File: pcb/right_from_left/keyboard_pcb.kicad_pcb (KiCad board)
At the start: 2 copper layers, 138.8 x 89.9 mm, 47 parts, among them J1 TRRS, J2 Conn_01x04_Male, K0 KEYSW, K1 KEYSW, K10 KEYSW, K11 KEYSW, K12 KEYSW, K13 KEYSW, K14 KEYSW, K15 KEYSW, K2 KEYSW, K20 KEYSW, K21 KEYSW, K22 KEYSW, K23 KEYSW, K24 KEYSW, K25 KEYSW, K3 KEYSW, K30 KEYSW, K31 KEYSW, K32 KEYSW, K4 KEYSW, K5 KEYSW, U1 PCF8574, U2 Pico

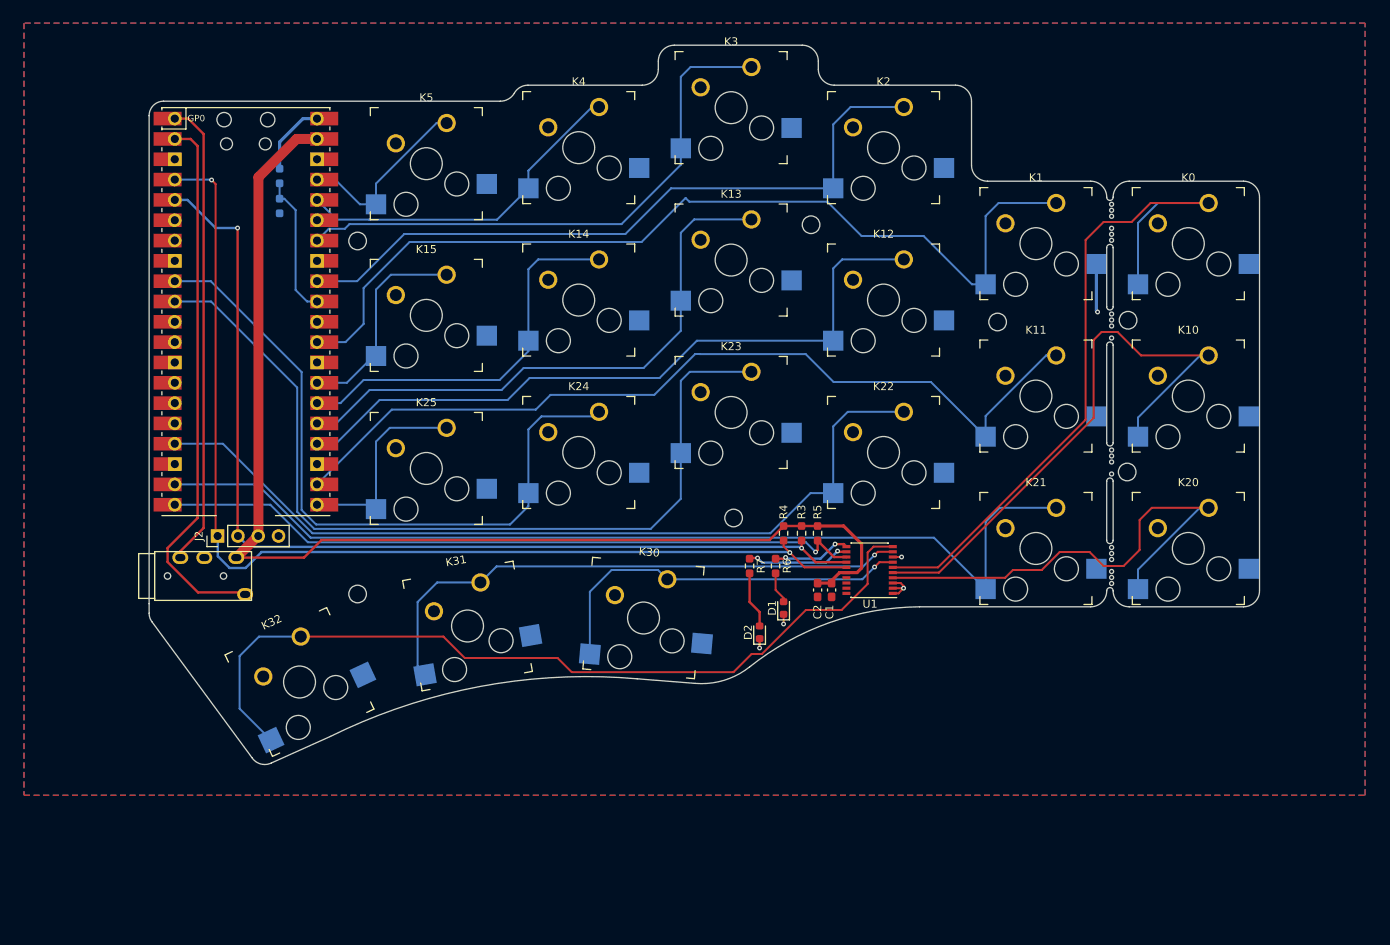
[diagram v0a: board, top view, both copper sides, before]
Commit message: right_from_left is ready for review
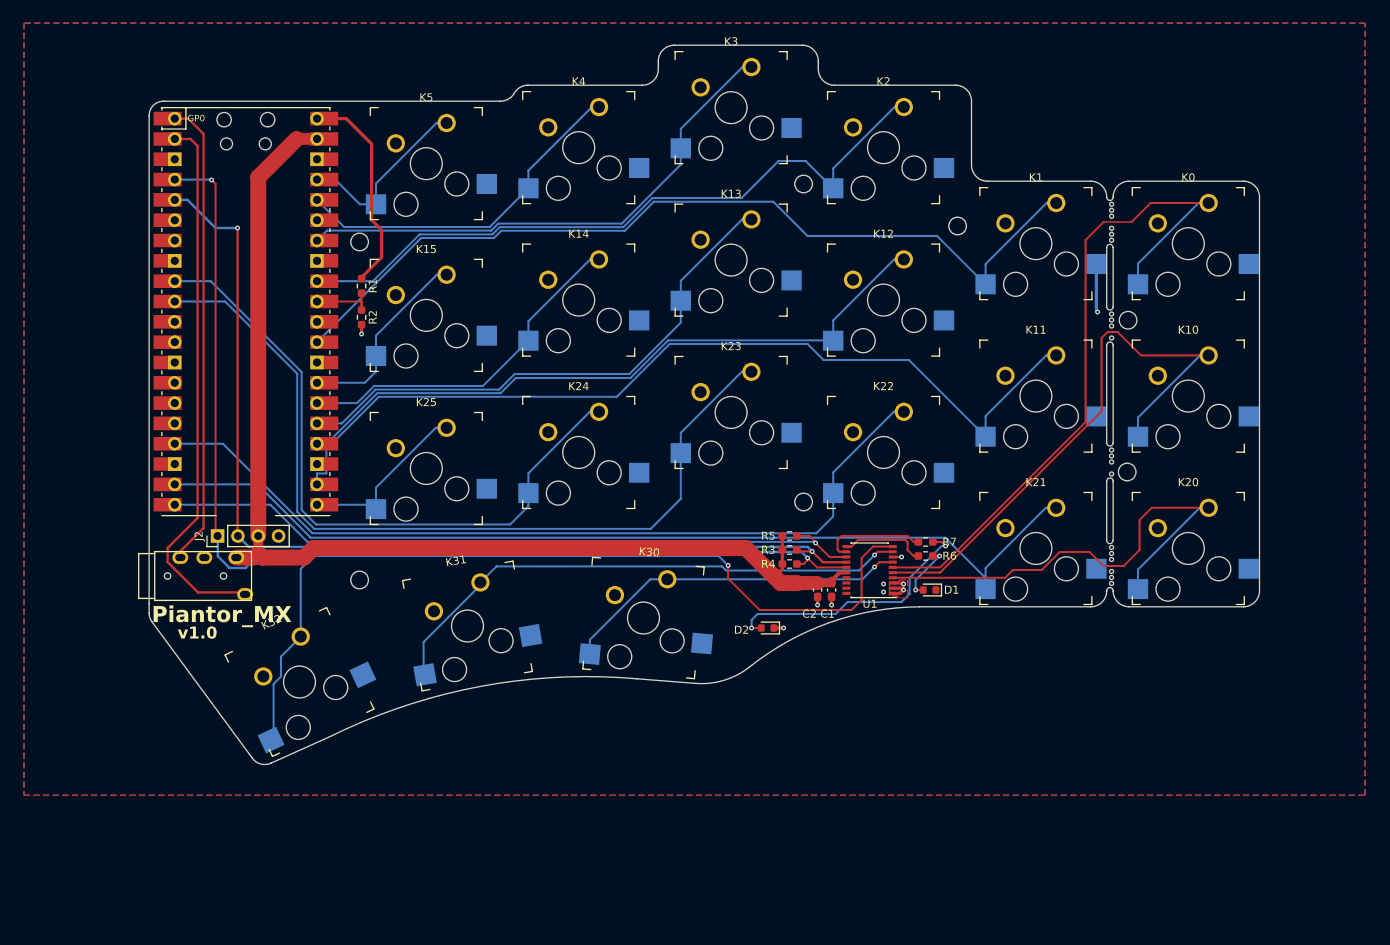
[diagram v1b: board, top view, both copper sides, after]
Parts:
- R1, R2: moved to F.Cu
- R3, R4: value R -> 4k7
- moved H1 29.8 mm to (148.2, 60.8)
- moved R7 22.2 mm to (163.5, 105.5), turned to 0 degrees
- moved R6 18.8 mm to (163.5, 107.2), turned to 0 degrees
- moved D1 18.4 mm to (164.0, 111.5), turned to 180 degrees
- moved H1 18.3 mm to (167.5, 66.0)
- moved R2 17.3 mm to (93.0, 77.4)
- moved R1 17.2 mm to (93.0, 73.5)
- moved H4 8.98 mm to (148.2, 100.5)
- moved R4 3.91 mm to (146.5, 108.2), turned to 0 degrees
- moved R5 3.52 mm to (146.5, 104.8), turned to 0 degrees
- moved R3 2.57 mm to (146.5, 106.5), turned to 0 degrees
- moved H3 1.77 mm to (92.8, 110.2)
- moved D2 1.14 mm to (143.8, 116.2), turned to 180 degrees
- moved H2 0.28 mm to (92.8, 68.0)
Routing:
- net Net-(D2-A): track 7.11 -> 33.3 mm, vias 0 -> 2
- net VBUS: track 9.22 -> 26.8 mm
- net vbus_sense: track 17.8 -> 8.69 mm
- net VCC: track 148.2 -> 141.6 mm
- net /k01: track 116.2 -> 109.6 mm
- net /k14: track 48.7 -> 44.1 mm
- net /k30: track 47.7 -> 43.2 mm
- net /k13: track 72.0 -> 67.9 mm
- net /k03: track 69.7 -> 65.9 mm
- net /k12: track 88.2 -> 84.4 mm
- net /k11: track 109.2 -> 112.8 mm
- net /k31: track 71.5 -> 68.1 mm
- net /k25: track 25.6 -> 22.2 mm
- net Net-(D1-A): track 3.96 -> 7.29 mm, vias 0 -> 2
- net /k24: track 87.2 -> 84.0 mm
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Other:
- board text added: "Piantor_MX"
- board text added: "v1.0"

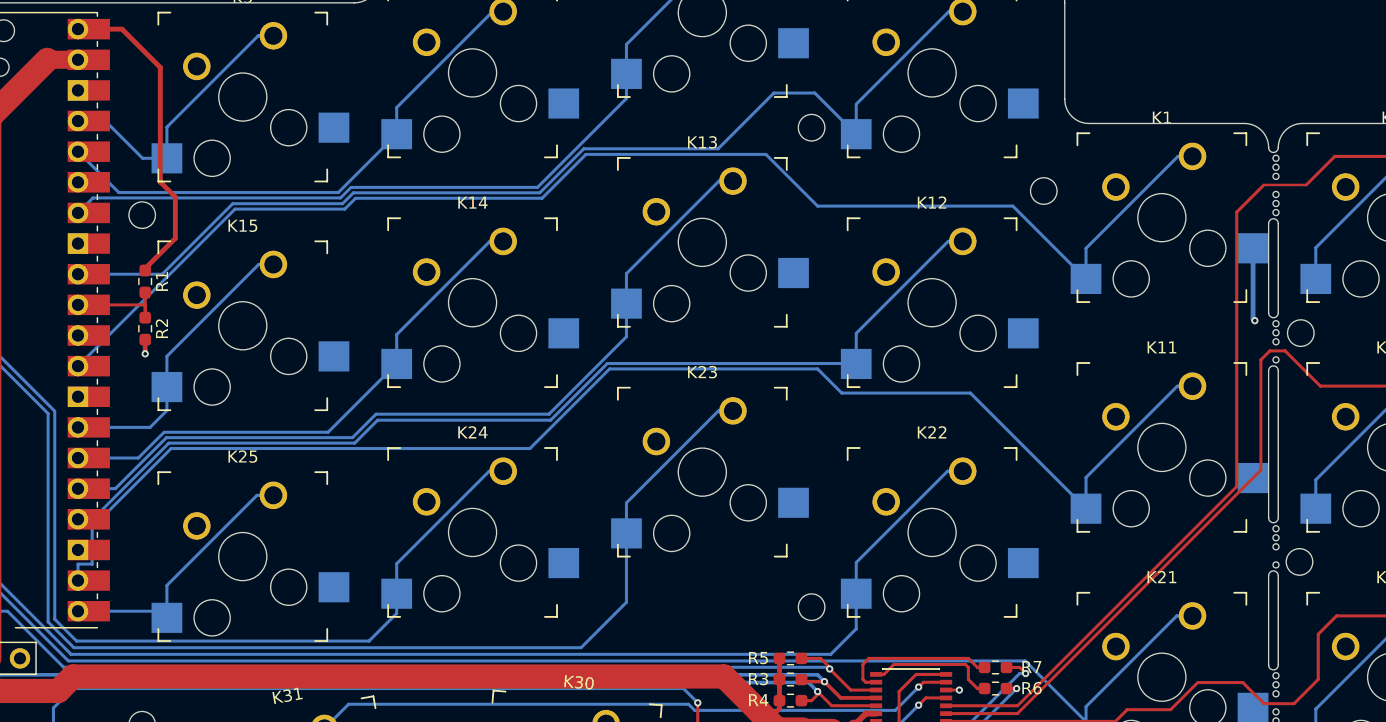
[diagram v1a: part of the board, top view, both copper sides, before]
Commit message: Mechanical parts are "mirrored", ToDo: Pin header LCD i2c pinheader needs alignment
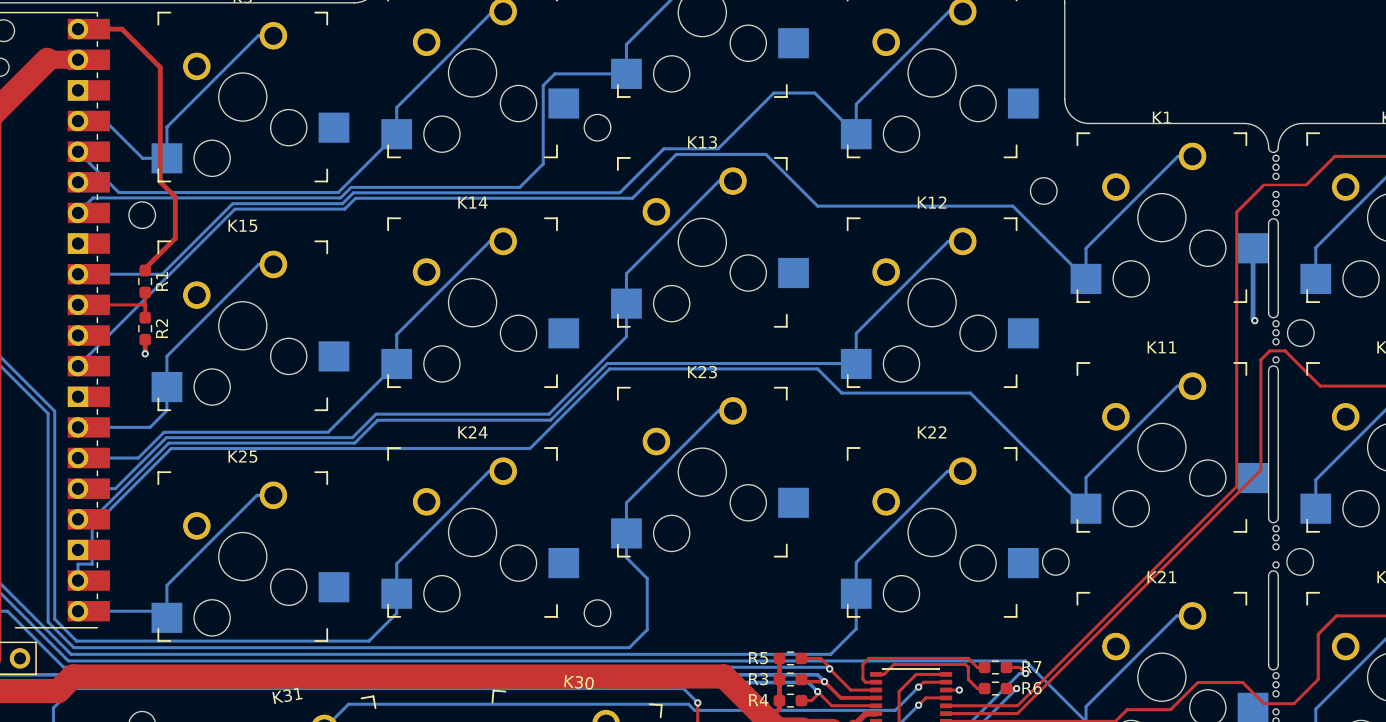
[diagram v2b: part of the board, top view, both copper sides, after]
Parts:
- added H4: MountingHole, beekeeb_lib:MountingHole_2.2mm_M2-8mm, B.Cu at (130.5, 101.0)
- moved H4 20.6 mm to (168.5, 96.8)
- moved H1 17.8 mm to (130.5, 60.8)
- moved H4 0.06 mm to (188.8, 96.8)
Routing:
- net /k23: track 106.9 -> 110.7 mm
- net /k03: track 65.9 -> 68.5 mm
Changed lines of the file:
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@@
   )
   (footprint "beekeeb_lib:MountingHole_2.2mm_M2-8mm" (layer "B.Cu")
-    (at 148.25 100.5 180)
+    (at 168.5 96.75 180)
     (descr "Mounting Hole 2.2mm, no annular, M2")
     (tags "mounting hole 2.2mm no annular m2")
@@
   )
   (footprint "beekeeb_lib:MountingHole_2.2mm_M2-8mm" (layer "B.Cu")
-    (at 188.75 96.75 180)
+    (at 188.808 96.75 180)
     (descr "Mounting Hole 2.2mm, no annular, M2")
     (tags "mounting hole 2.2mm no annular m2")
@@
   )
   (footprint "beekeeb_lib:MountingHole_2.2mm_M2-8mm" (layer "B.Cu")
-    (at 148.25 60.75 180)
+    (at 130.5 101 180)
+    (descr "Mounting Hole 2.2mm, no annular, M2")
+    (tags "mounting hole 2.2mm no annular m2")
+    (property "Sheetfile" "keyboard_pcb.kicad_sch")
+    (property "Sheetname" "")
+    (property "ki_description" "Mounting Hole without connection")
+    (property "ki_keywords" "mounting hole")
+    (attr exclude_from_pos_files)
+    (fp_text reference "H4" (at 0 3.2) (layer "B.SilkS") hide
+        (effects (font (size 1 1) (thickness 0.15)) (justify mirror))
+    )
+    (fp_text value "MountingHole" (at 2.335 -4.852) (layer "B.Fab")
+        (effects (font (size 1 1) (thickness 0.15)) (justify mirror))
+    )
+    (fp_text user "${REFERENCE}" (at 0 0) (layer "B.Fab")
+        (effects (font (size 1 1) (thickness 0.15)) (justify mirror))
+    )
+    (fp_circle (center 0 0) (end 2.2 0)
+      (stroke (width 0.15) (type solid)) (fill none) (layer "Cmts.User"))
+    (fp_circle (center 0 0) (end 4 0)
+      (stroke (width 0.05) (type solid)) (fill none) (layer "B.CrtYd"))
+    (pad "" np_thru_hole circle (at 0 0 180) (size 2.2 2.2) (drill 2.2) (layers "*.Cu" "*.Mask"))
+  )
+  (footprint "beekeeb_lib:MountingHole_2.2mm_M2-8mm" (layer "B.Cu")
+    (at 130.5 60.75 180)
     (descr "Mounting Hole 2.2mm, no annular, M2")
     (tags "mounting hole 2.2mm no annular m2")
@@
   (segment (start 197.622 63.128) (end 198.88 63.128) (width 0.25) (layer "B.Cu") (net 2))
   (segment (start 190.05 70.7) (end 197.622 63.128) (width 0.25) (layer "B.Cu") (net 2))
-  (segment (start 100.4448 67.5) (end 109.54507 67.5) (width 0.25) (layer "B.Cu") (net 3))
-  (segment (start 110.446567 66.598503) (end 125.901497 66.598503) (width 0.25) (layer "B.Cu") (net 3))
-  (segment (start 170.975 73.288) (end 171 73.288) (width 0.25) (layer "B.Cu") (net 3))
+  (segment (start 137.037 62.963) (end 144.463 62.963) (width 0.25) (layer "B.Cu") (net 3))
+  (segment (start 110.446567 66.598503) (end 133.401497 66.598503) (width 0.25) (layer "B.Cu") (net 3))
   (segment (start 109.54507 67.5) (end 110.446567 66.598503) (width 0.25) (layer "B.Cu") (net 3))
   (segment (start 148.75 67.25) (end 164.937 67.25) (width 0.25) (layer "B.Cu") (net 3))
-  (segment (start 125.901497 66.598503) (end 129.537 62.963) (width 0.25) (layer "B.Cu") (net 3))
+  (segment (start 170.975 73.288) (end 171 73.288) (width 0.25) (layer "B.Cu") (net 3))
+  (segment (start 100.4448 67.5) (end 109.54507 67.5) (width 0.25) (layer "B.Cu") (net 3))
+  (segment (start 87.4268 80.518) (end 100.4448 67.5) (width 0.25) (layer "B.Cu") (net 3))
+  (segment (start 144.463 62.963) (end 148.75 67.25) (width 0.25) (layer "B.Cu") (net 3))
+  (segment (start 133.401497 66.598503) (end 137.037 62.963) (width 0.25) (layer "B.Cu") (net 3))
   (segment (start 164.937 67.25) (end 170.975 73.288) (width 0.25) (layer "B.Cu") (net 3))
-  (segment (start 144.463 62.963) (end 148.75 67.25) (width 0.25) (layer "B.Cu") (net 3))
-  (segment (start 87.4268 80.518) (end 100.4448 67.5) (width 0.25) (layer "B.Cu") (net 3))
-  (segment (start 129.537 62.963) (end 144.463 62.963) (width 0.25) (layer "B.Cu") (net 3))
   (segment (start 171 70.75) (end 178.622 63.128) (width 0.25) (layer "B.Cu") (net 3))
   (segment (start 178.622 63.128) (end 179.83 63.128) (width 0.25) (layer "B.Cu") (net 3))
   (segment (start 171 73.288) (end 171 70.75) (width 0.25) (layer "B.Cu") (net 3))
+  (segment (start 140.5 62.5) (end 145.125 57.875) (width 0.25) (layer "B.Cu") (net 4))
   (segment (start 151.95 61.288) (end 151.95 58.8) (width 0.25) (layer "B.Cu") (net 4))
-  (segment (start 140.5 62.5) (end 145.125 57.875) (width 0.25) (layer "B.Cu") (net 4))
+  (segment (start 148.512 57.875) (end 151.925 61.288) (width 0.25) (layer "B.Cu") (net 4))
+  (segment (start 109.358881 67.050499) (end 110.260378 66.149002) (width 0.25) (layer "B.Cu") (net 4))
   (segment (start 145.125 57.875) (end 148.512 57.875) (width 0.25) (layer "B.Cu") (net 4))
+  (segment (start 132.350998 66.149002) (end 136 62.5) (width 0.25) (layer "B.Cu") (net 4))
   (segment (start 94.41111 72.898) (end 100.258611 67.050499) (width 0.25) (layer "B.Cu") (net 4))
-  (segment (start 148.512 57.875) (end 151.925 61.288) (width 0.25) (layer "B.Cu") (net 4))
   (segment (start 151.925 61.288) (end 151.95 61.288) (width 0.25) (layer "B.Cu") (net 4))
-  (segment (start 109.358881 67.050499) (end 110.260378 66.149002) (width 0.25) (layer "B.Cu") (net 4))
-  (segment (start 110.260378 66.149002) (end 125.715308 66.149002) (width 0.25) (layer "B.Cu") (net 4))
+  (segment (start 136 62.5) (end 140.5 62.5) (width 0.25) (layer "B.Cu") (net 4))
+  (segment (start 159.622 51.128) (end 160.78 51.128) (width 0.25) (layer "B.Cu") (net 4))
+  (segment (start 100.258611 67.050499) (end 109.358881 67.050499) (width 0.25) (layer "B.Cu") (net 4))
+  (segment (start 151.95 58.8) (end 159.622 51.128) (width 0.25) (layer "B.Cu") (net 4))
   (segment (start 87.4268 72.898) (end 94.41111 72.898) (width 0.25) (layer "B.Cu") (net 4))
-  (segment (start 159.622 51.128) (end 160.78 51.128) (width 0.25) (layer "B.Cu") (net 4))
-  (segment (start 151.95 58.8) (end 159.622 51.128) (width 0.25) (layer "B.Cu") (net 4))
-  (segment (start 125.715308 66.149002) (end 129.36431 62.5) (width 0.25) (layer "B.Cu") (net 4))
-  (segment (start 100.258611 67.050499) (end 109.358881 67.050499) (width 0.25) (layer "B.Cu") (net 4))
-  (segment (start 129.36431 62.5) (end 140.5 62.5) (width 0.25) (layer "B.Cu") (net 4))
+  (segment (start 110.260378 66.149002) (end 132.350998 66.149002) (width 0.25) (layer "B.Cu") (net 4))
+  (segment (start 124.050499 65.699501) (end 126 63.75) (width 0.25) (layer "B.Cu") (net 5))
+  (segment (start 109.19869 66.575) (end 110.074189 65.699501) (width 0.25) (layer "B.Cu") (net 5))
+  (segment (start 132.9 53.85) (end 140.622 46.128) (width 0.25) (layer "B.Cu") (net 5))
   (segment (start 88.6698 66.575) (end 109.19869 66.575) (width 0.25) (layer "B.Cu") (net 5))
-  (segment (start 132.9 53.85) (end 140.622 46.128) (width 0.25) (layer "B.Cu") (net 5))
+  (segment (start 126 57.25) (end 126.962 56.288) (width 0.25) (layer "B.Cu") (net 5))
+  (segment (start 126.962 56.288) (end 132.9 56.288) (width 0.25) (layer "B.Cu") (net 5))
+  (segment (start 126 63.75) (end 126 57.25) (width 0.25) (layer "B.Cu") (net 5))
+  (segment (start 132.9 56.288) (end 132.9 53.85) (width 0.25) (layer "B.Cu") (net 5))
+  (segment (start 110.074189 65.699501) (end 124.050499 65.699501) (width 0.25) (layer "B.Cu") (net 5))
   (segment (start 87.4268 67.818) (end 88.6698 66.575) (width 0.25) (layer "B.Cu") (net 5))
-  (segment (start 132.9 56.288) (end 132.9 53.85) (width 0.25) (layer "B.Cu") (net 5))
-  (segment (start 110.074189 65.699501) (end 125.529119 65.699501) (width 0.25) (layer "B.Cu") (net 5))
-  (segment (start 109.19869 66.575) (end 110.074189 65.699501) (width 0.25) (layer "B.Cu") (net 5))
-  (segment (start 125.529119 65.699501) (end 132.9 58.32862) (width 0.25) (layer "B.Cu") (net 5))
-  (segment (start 132.9 58.32862) (end 132.9 56.288) (width 0.25) (layer "B.Cu") (net 5))
   (segment (start 140.622 46.128) (end 141.73 46.128) (width 0.25) (layer "B.Cu") (net 5))
   (segment (start 87.4268 62.738) (end 90.814299 66.125499) (width 0.25) (layer "B.Cu") (net 6))
@@
   (segment (start 151.95 99.388) (end 151.95 96.8) (width 0.25) (layer "B.Cu") (net 16))
   (segment (start 151.95 96.8) (end 159.522 89.228) (width 0.25) (layer "B.Cu") (net 16))
-  (segment (start 69.6468 75.438) (end 75.938 75.438) (width 0.25) (layer "B.Cu") (net 17))
+  (segment (start 84.950499 101.726905) (end 87.086095 103.862501) (width 0.25) (layer "B.Cu") (net 17))
+  (segment (start 134.625 98.125) (end 132.9 96.4) (width 0.25) (layer "B.Cu") (net 17))
+  (segment (start 87.086095 103.862501) (end 133.137499 103.862501) (width 0.25) (layer "B.Cu") (net 17))
+  (segment (start 134.625 102.375) (end 134.625 98.125) (width 0.25) (layer "B.Cu") (net 17))
+  (segment (start 133.137499 103.862501) (end 134.625 102.375) (width 0.25) (layer "B.Cu") (net 17))
   (segment (start 75.938 75.438) (end 84.950499 84.450499) (width 0.25) (layer "B.Cu") (net 17))
-  (segment (start 87.086095 103.862501) (end 129.137499 103.862501) (width 0.25) (layer "B.Cu") (net 17))
-  (segment (start 132.9 100.1) (end 132.9 94.388) (width 0.25) (layer "B.Cu") (net 17))
   (segment (start 132.9 91.85) (end 132.9 94.388) (width 0.25) (layer "B.Cu") (net 17))
   (segment (start 84.950499 84.450499) (end 84.950499 101.726905) (width 0.25) (layer "B.Cu") (net 17))
-  (segment (start 129.137499 103.862501) (end 132.9 100.1) (width 0.25) (layer "B.Cu") (net 17))
-  (segment (start 84.950499 101.726905) (end 87.086095 103.862501) (width 0.25) (layer "B.Cu") (net 17))
   (segment (start 141.73 84.228) (end 140.522 84.228) (width 0.25) (layer "B.Cu") (net 17))
   (segment (start 140.522 84.228) (end 132.9 91.85) (width 0.25) (layer "B.Cu") (net 17))
+  (segment (start 132.9 96.4) (end 132.9 94.388) (width 0.25) (layer "B.Cu") (net 17))
+  (segment (start 69.6468 75.438) (end 75.938 75.438) (width 0.25) (layer "B.Cu") (net 17))
   (segment (start 121.522 89.228) (end 122.68 89.228) (width 0.25) (layer "B.Cu") (net 18))
   (segment (start 85.5 84.25) (end 74.148 72.898) (width 0.25) (layer "B.Cu") (net 18))
